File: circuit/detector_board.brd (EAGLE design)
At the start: 45 x 48.5 mm, 10 parts

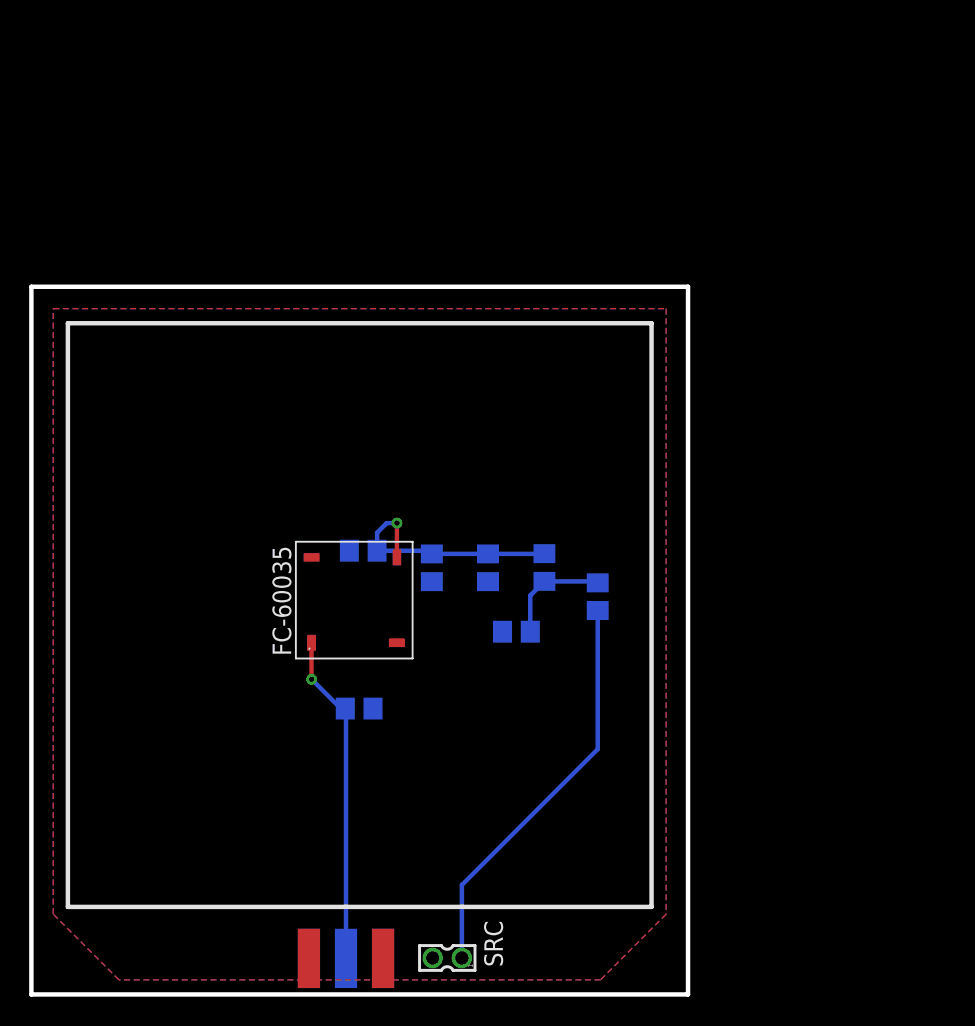
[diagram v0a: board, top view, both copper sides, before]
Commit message: boards; docs: Updated docs with impedance calculator; updated board design to stack, be solderable, and use new package design for FC-600XX.
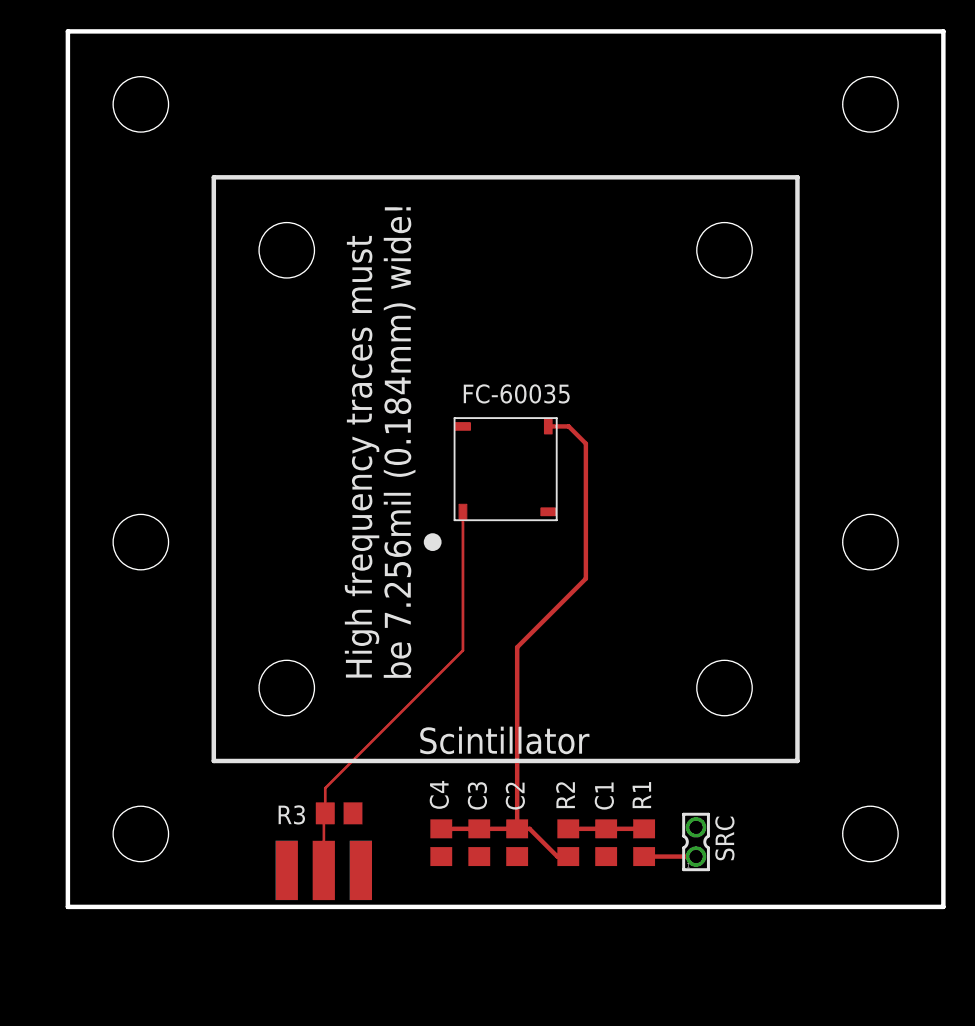
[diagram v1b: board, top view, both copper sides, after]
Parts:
- moved C4 20.7 mm to (25.6, 4.40), flipped to the top, turned to 270 degrees
- moved C3 19.1 mm to (28.2, 4.40), flipped to the top
- moved C2 18.9 mm to (30.8, 4.40), flipped to the top
- moved R2 18.9 mm to (34.3, 4.40), flipped to the top, turned to 270 degrees
- moved SRC 18.8 mm to (43.0, 4.45), turned to 0 degrees
- moved FC-60035 17.8 mm to (30.0, 30.0)
- moved R1 17.2 mm to (39.5, 4.40), flipped to the top
- moved C1 15.7 mm to (36.9, 4.40), flipped to the top, turned to 270 degrees
- moved J$1 8.94 mm to (15.0, 2.50), flipped to the top
- moved R3 7.31 mm to (18.6, 6.41), flipped to the top, turned to 180 degrees
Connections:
- net N$2 renamed VBIAS
- net N$3 renamed V_AN
- net GND: now also FC-60035.F_FAST
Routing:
- net VBIAS: track 16.8 -> 41.1 mm, vias 1 -> 0
- net N$4: track 27.7 -> 3.56 mm
- net V_AN: track 22.8 -> 28.5 mm, vias 1 -> 0
- net N$1: track 7.54 -> 5.20 mm
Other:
- board size 45 x 48.5 mm -> 60 x 60 mm
- board text added: "High frequency traces must be 7.256mil (0.184mm) wide!"
- board text added: "Scintillator"

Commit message: boards: Changes to library and board designs.
Will I need to remove the vias and replace them with holes in order to be able to ground both sides?
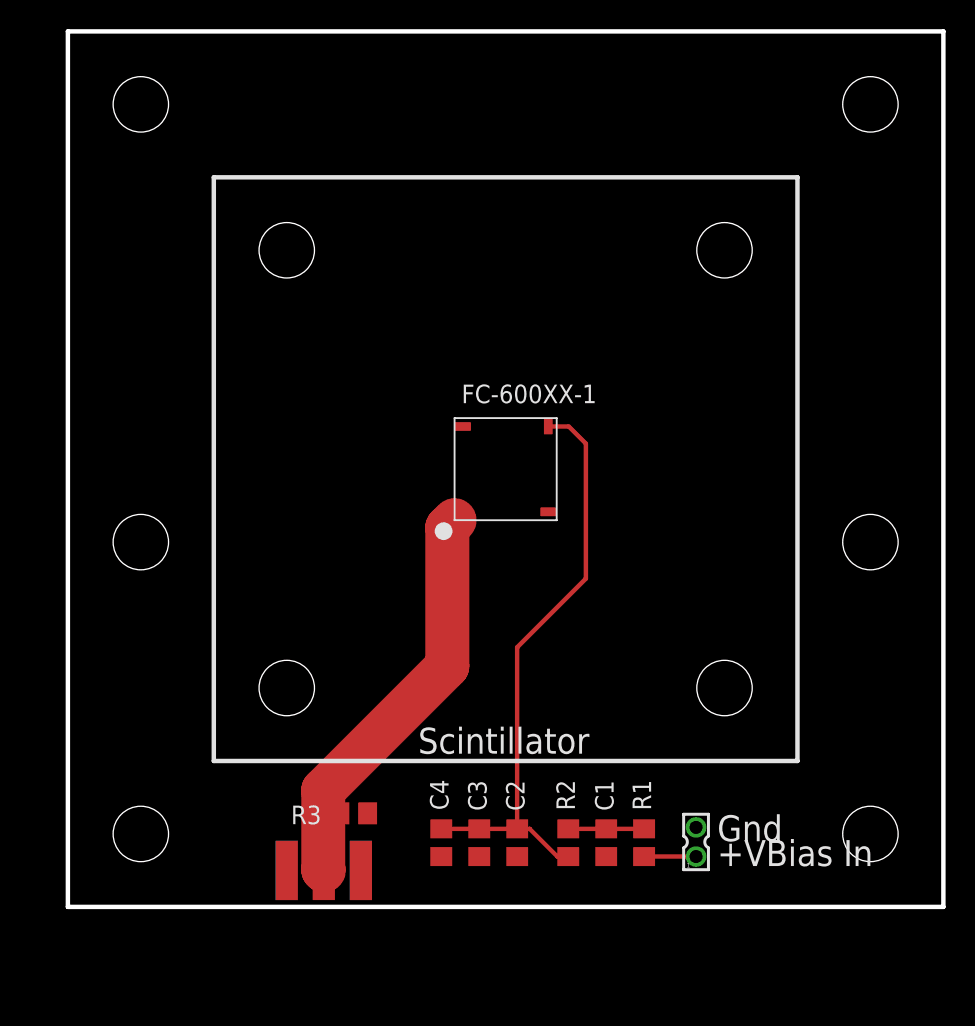
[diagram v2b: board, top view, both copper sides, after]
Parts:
- removed FC-60035: FC-600XXSMT_REFLOW, 000phys605parts:FC-600XX-SMT
- added FC-600XX-1: FC-600XXBLANK, 000phys605parts:FC-600XX-SMT_BLANK5
- moved R3 1.00 mm to (19.6, 6.41)
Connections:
- net GND: now also FC-600XX-1.NC; no longer FC-60035.F_FAST
- net VBIAS: now also FC-600XX-1.N_CATH; no longer FC-60035.N_CATH
- net V_AN: now also FC-600XX-1.P_AN; no longer FC-60035.P_AN
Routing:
- net V_AN: track 28.5 -> 29.7 mm
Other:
- board text added: "+VBias In"
- board text added: "Gnd"
- board text removed: "High frequency traces must be 7.256mil (0.184mm) wide!"
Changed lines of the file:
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@@
 <drawing>
 <settings>
-<setting alwaysvectorfont="yes"/>
+<setting alwaysvectorfont="no"/>
 <setting verticaltext="up"/>
 </settings>
@@
 <hole x="55" y="55" drill="3.7973"/>
 <hole x="5" y="55" drill="3.7973"/>
-<text x="23.5" y="15.5" size="1.778" layer="21" rot="R90">High frequency traces must
-be 7.256mil (0.184mm) wide!</text>
 <hole x="5" y="25" drill="3.7973"/>
 <hole x="55" y="25" drill="3.7973"/>
+<text x="44.5" y="2.8" size="1.778" layer="21">+VBias In</text>
+<text x="44.5" y="4.5" size="1.778" layer="21">Gnd</text>
 </plain>
 <attributes>
@@
 <clearance class="0" value="0.3048"/>
 </class>
-<class number="1" name="high_freq" width="0.184303125" drill="0">
+<class number="1" name="high_freq" width="3.021" drill="0">
 <clearance class="0" value="0.508"/>
 <clearance class="1" value="0.508"/>
@@
 <attribute name="SPICEPREFIX" value="R" x="34.29" y="4.4" size="1.778" layer="27" rot="R270" display="off"/>
 </element>
-<element name="R3" library="rcl" library_urn="urn:adsk.eagle:library:334" package="R0805" package3d_urn="urn:adsk.eagle:package:23553/2" value="49.9" x="18.59" y="6.41" smashed="yes" rot="R180">
-<attribute name="NAME" x="16.375" y="6.94" size="1.27" layer="25" rot="R180"/>
-<attribute name="SPICEPREFIX" value="R" x="18.59" y="6.41" size="1.778" layer="27" rot="R180" display="off"/>
+<element name="R3" library="rcl" library_urn="urn:adsk.eagle:library:334" package="R0805" package3d_urn="urn:adsk.eagle:package:23553/2" value="49.9" x="19.59" y="6.41" smashed="yes" rot="R180">
+<attribute name="NAME" x="17.375" y="6.94" size="1.27" layer="25" rot="R180"/>
+<attribute name="SPICEPREFIX" value="R" x="19.59" y="6.41" size="1.778" layer="27" rot="R180" display="off"/>
 </element>
 <element name="C1" library="rcl" package="C0805" value="10nF" x="36.89" y="4.4" smashed="yes" rot="R270">
@@
 <element name="J$1" library="SparkFun-Retired" package="SMA-EDGE" value="SMA_EDGE" x="15" y="2.5"/>
 <element name="SRC" library="con-garry" library_urn="urn:adsk.eagle:library:147" package="332-02" package3d_urn="urn:adsk.eagle:package:6810/1" value="" x="43.05" y="4.45" smashed="yes">
-<attribute name="NAME" x="44.39" y="6.27" size="1.27" layer="25" rot="R270"/>
 <attribute name="VALUE" x="42.43" y="6.99" size="1.27" layer="27"/>
 </element>
-<element name="FC-60035" library="000phys605parts" package="FC-600XX-SMT" value="FC-600XXSMT_REFLOW" x="30" y="30" smashed="yes">
-<attribute name="NAME" x="26.9774" y="34.5212" size="1.27" layer="25"/>
-</element>
+<element name="FC-600XX-1" library="000phys605parts" package="FC-600XX-SMT_BLANK5" value="FC-600XXBLANK" x="30" y="30"/>
 </elements>
 <signals>
@@
 <wire x1="30.79" y1="17.79" x2="35.5" y2="22.5" width="0.3048" layer="1"/>
 <wire x1="35.5" y1="22.5" x2="35.5" y2="31.752" width="0.3048" layer="1"/>
-<contactref element="FC-60035" pad="N_CATH"/>
-<wire x1="35.5" y1="31.752" x2="34.327" y2="32.925" width="0.305" layer="1"/>
-<wire x1="34.327" y1="32.925" x2="32.925" y2="32.925" width="0.305" layer="1"/>
+<wire x1="34.327" y1="32.925" x2="35.5" y2="31.752" width="0.305" layer="1"/>
+<contactref element="FC-600XX-1" pad="N_CATH"/>
+<wire x1="32.925" y1="32.925" x2="34.327" y2="32.925" width="0.3048" layer="1"/>
 </signal>
 <signal name="GND">
@@
 <vertex x="0" y="0"/>
 </polygon>
-<contactref element="FC-60035" pad="F_FAST"/>
+<contactref element="FC-600XX-1" pad="NC"/>
 </signal>
 <signal name="V_AN" class="1">
 <contactref element="R3" pad="2"/>
 <contactref element="J$1" pad="SIG"/>
-<wire x1="17.54" y1="6.31" x2="17.54" y2="2.5" width="0.184" layer="1"/>
-<wire x1="17.64" y1="8.14" x2="27.075" y2="17.575" width="0.184" layer="1"/>
-<wire x1="17.64" y1="6.41" x2="17.64" y2="8.14" width="0.184" layer="1"/>
-<contactref element="FC-60035" pad="P_AN"/>
-<wire x1="27.075" y1="27.075" x2="27.075" y2="17.575" width="0.184" layer="1"/>
-<wire x1="17.64" y1="6.41" x2="17.54" y2="6.31" width="0.305" layer="1"/>
+<wire x1="17.5" y1="6.5" x2="17.5" y2="8" width="3.021" layer="1"/>
+<wire x1="17.5" y1="8" x2="25.997071875" y2="16.497071875" width="3.021" layer="1"/>
+<wire x1="25.997071875" y1="16.497071875" x2="26" y2="16.504140625" width="3.021" layer="1" curve="44.982095"/>
+<wire x1="26" y1="16.504140625" x2="26" y2="26" width="3.021" layer="1"/>
+<contactref element="FC-600XX-1" pad="P_AN"/>
+<wire x1="26.5" y1="26.5" x2="27.075" y2="27.075" width="0.3048" layer="1"/>
+<wire x1="18.64" y1="6.41" x2="18.55" y2="6.5" width="0.3048" layer="1"/>
+<wire x1="18.55" y1="6.5" x2="17.5" y2="6.5" width="0.3048" layer="1"/>
+<wire x1="17.54" y1="2.5" x2="17.5" y2="2.54" width="3.021" layer="1"/>
+<wire x1="17.5" y1="2.54" x2="17.5" y2="6.5" width="3.021" layer="1"/>
+<wire x1="26" y1="26" x2="26.5" y2="26.5" width="3.021" layer="1"/>
 </signal>
 <signal name="N$4">
@@
 </drawing>
 <compatibility>
-<note version="6.3" minversion="6.2.2" severity="warning">
-Since Version 6.2.2 text objects can contain more than one line,
-which will not be processed correctly with this version.
-</note>
 <note version="8.2" severity="warning">
 Since Version 8.2, EAGLE supports online libraries. The ids

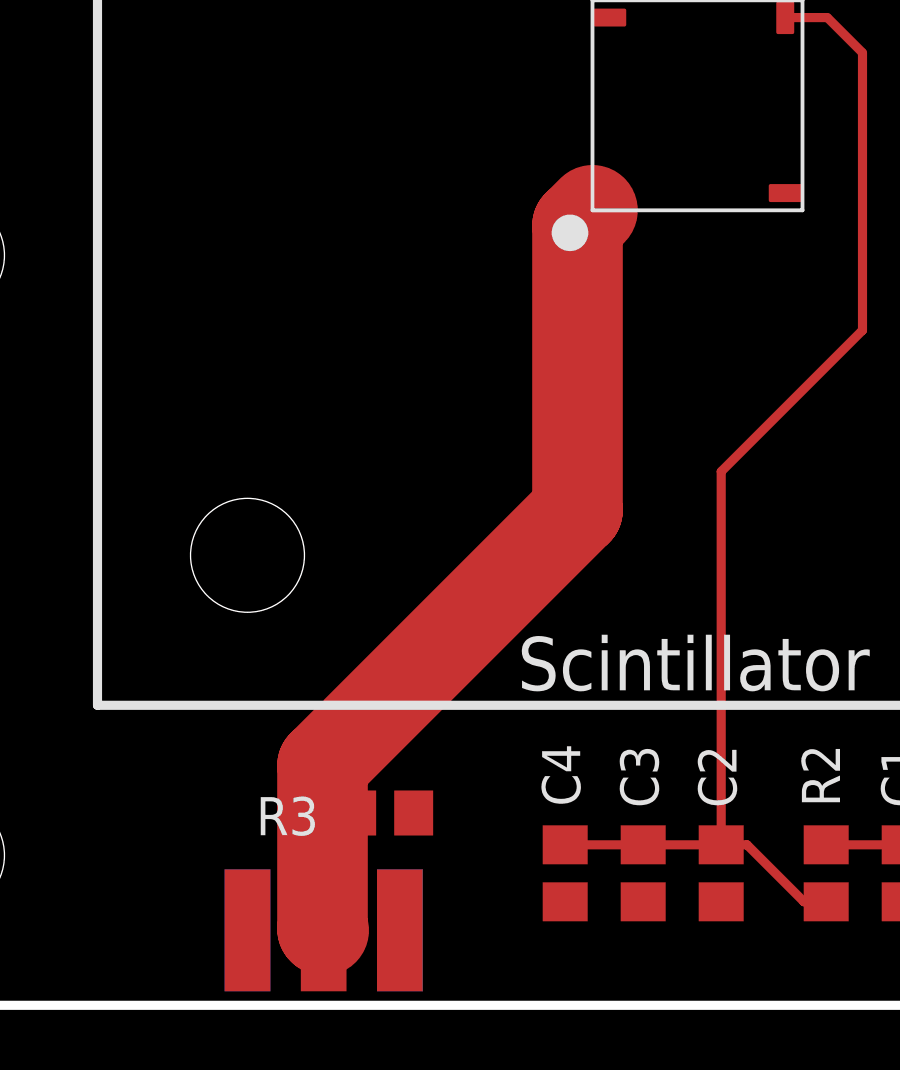
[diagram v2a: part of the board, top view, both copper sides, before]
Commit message: boards: Simplified both boards
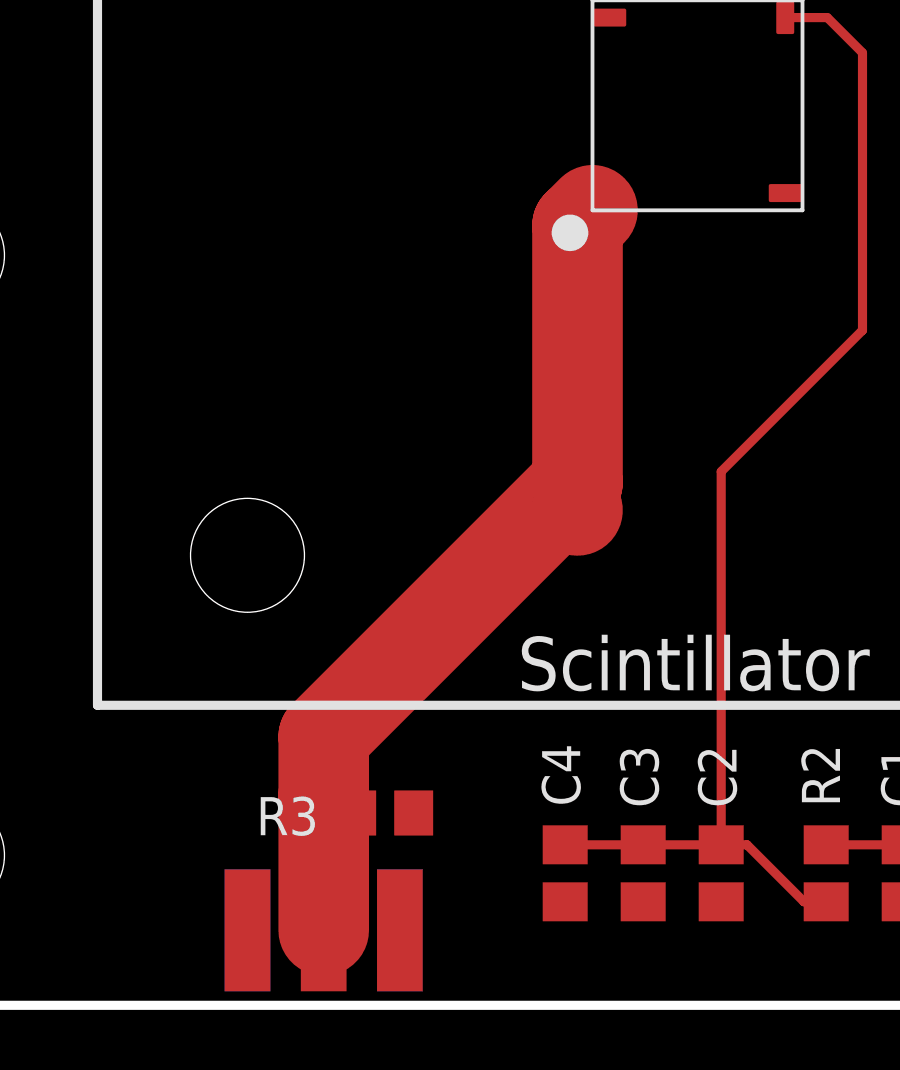
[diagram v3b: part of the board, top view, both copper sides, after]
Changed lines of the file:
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@@
 <contactref element="R3" pad="2"/>
 <contactref element="J$1" pad="SIG"/>
-<wire x1="17.5" y1="6.5" x2="17.5" y2="8" width="3.021" layer="1"/>
-<wire x1="17.5" y1="8" x2="25.997071875" y2="16.497071875" width="3.021" layer="1"/>
 <wire x1="25.997071875" y1="16.497071875" x2="26" y2="16.504140625" width="3.021" layer="1" curve="44.982095"/>
-<wire x1="26" y1="16.504140625" x2="26" y2="26" width="3.021" layer="1"/>
 <contactref element="FC-600XX-1" pad="P_AN"/>
 <wire x1="26.5" y1="26.5" x2="27.075" y2="27.075" width="0.3048" layer="1"/>
-<wire x1="18.64" y1="6.41" x2="18.55" y2="6.5" width="0.3048" layer="1"/>
-<wire x1="18.55" y1="6.5" x2="17.5" y2="6.5" width="0.3048" layer="1"/>
-<wire x1="17.54" y1="2.5" x2="17.5" y2="2.54" width="3.021" layer="1"/>
-<wire x1="17.5" y1="2.54" x2="17.5" y2="6.5" width="3.021" layer="1"/>
 <wire x1="26" y1="26" x2="26.5" y2="26.5" width="3.021" layer="1"/>
+<wire x1="17.54" y1="2.5" x2="17.54" y2="7" width="3.021" layer="1"/>
+<wire x1="17.54" y1="7" x2="17.54" y2="8.96" width="3.021" layer="1"/>
+<wire x1="17.54" y1="8.96" x2="26" y2="17.42" width="3.021" layer="1"/>
+<wire x1="26" y1="17.42" x2="26" y2="26" width="3.021" layer="1"/>
+<wire x1="18.64" y1="6.41" x2="18.05" y2="7" width="0.3048" layer="1"/>
+<wire x1="18.05" y1="7" x2="17.54" y2="7" width="0.3048" layer="1"/>
+<wire x1="26" y1="17.42" x2="26" y2="16.504140625" width="0" layer="19" extent="1-1"/>
 </signal>
 <signal name="N$4">

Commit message: boards: Rev00_ss ready
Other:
- board text added: "Rev00_ss, detector board Asher Merrill & Maurik Holtrop, UNH 2018"
- board text added: "Vbias"
- board text removed: "+VBias In"
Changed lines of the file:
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@@
 <setting verticaltext="up"/>
 </settings>
-<grid distance="0.5" unitdist="mm" unit="mm" style="dots" multiple="1" display="yes" altdistance="0.05" altunitdist="mm" altunit="mm"/>
+<grid distance="0.5" unitdist="mm" unit="mm" style="lines" multiple="1" display="yes" altdistance="0.05" altunitdist="mm" altunit="mm"/>
 <layers>
 <layer number="1" name="Top" color="4" fill="1" visible="yes" active="yes"/>
@@
 <hole x="5" y="25" drill="3.7973"/>
 <hole x="55" y="25" drill="3.7973"/>
-<text x="44.5" y="2.8" size="1.778" layer="21">+VBias In</text>
+<text x="44.5" y="2.5" size="1.778" layer="21">Vbias</text>
 <text x="44.5" y="4.5" size="1.778" layer="21">Gnd</text>
+<text x="43" y="58" size="1.2" layer="21" rot="R180">Rev00_ss, detector board
+Asher Merrill &amp; Maurik Holtrop, UNH 2018</text>
 </plain>
 <attributes>
@@
 <contactref element="R3" pad="2"/>
 <contactref element="J$1" pad="SIG"/>
-<wire x1="25.997071875" y1="16.497071875" x2="26" y2="16.504140625" width="3.021" layer="1" curve="44.982095"/>
 <contactref element="FC-600XX-1" pad="P_AN"/>
 <wire x1="26.5" y1="26.5" x2="27.075" y2="27.075" width="0.3048" layer="1"/>
-<wire x1="26" y1="26" x2="26.5" y2="26.5" width="3.021" layer="1"/>
+<wire x1="26.5" y1="26.5" x2="26" y2="26" width="3.021" layer="1"/>
 <wire x1="17.54" y1="2.5" x2="17.54" y2="7" width="3.021" layer="1"/>
 <wire x1="17.54" y1="7" x2="17.54" y2="8.96" width="3.021" layer="1"/>
-<wire x1="17.54" y1="8.96" x2="26" y2="17.42" width="3.021" layer="1"/>
-<wire x1="26" y1="17.42" x2="26" y2="26" width="3.021" layer="1"/>
+<wire x1="26" y1="17.42" x2="17.54" y2="8.96" width="3.021" layer="1"/>
 <wire x1="18.64" y1="6.41" x2="18.05" y2="7" width="0.3048" layer="1"/>
 <wire x1="18.05" y1="7" x2="17.54" y2="7" width="0.3048" layer="1"/>
-<wire x1="26" y1="17.42" x2="26" y2="16.504140625" width="0" layer="19" extent="1-1"/>
+<wire x1="26" y1="26" x2="26" y2="17.42" width="3.021" layer="1"/>
 </signal>
 <signal name="N$4">
@@
 </drawing>
 <compatibility>
+<note version="6.3" minversion="6.2.2" severity="warning">
+Since Version 6.2.2 text objects can contain more than one line,
+which will not be processed correctly with this version.
+</note>
 <note version="8.2" severity="warning">
 Since Version 8.2, EAGLE supports online libraries. The ids
